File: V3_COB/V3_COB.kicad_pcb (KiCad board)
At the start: 4 copper layers, 16 x 16 mm, 3 parts, among them J101 Conn_02x35_Counter_Clockwise_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, J102 Conn_2Rows-76Pins

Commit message: XP update in V3_COB (clean up works)
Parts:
- removed J102: Conn_2Rows-76Pins, MOSBius_V2_CHIP:round_COB
- added J1: Conn_2Rows-76Pins, MOSBius_V2_CHIP:round_COB, F.Cu at (204.2, 63.5)
- moved G*** 2.25 mm to (211.2, 56.8)
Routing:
- net GND: track 46.7 -> 22.8 mm, vias 23 -> 4
- net /PIN 15: track 10.2 -> 6.47 mm
- net /PIN 13: track 10.1 -> 6.42 mm
- net /PIN 11: track 9.58 -> 6.14 mm
- net /PIN 56: track 8.49 -> 5.76 mm
- net /PIN 53: track 9.25 -> 6.63 mm
- net /PIN 12: track 7.82 -> 5.91 mm
- net /PIN 55: track 8.63 -> 7.02 mm
- net /PIN 41: track 7.76 -> 6.17 mm
- net /PIN 52: track 7.36 -> 5.84 mm
- net /PIN 46: track 6.46 -> 7.82 mm
- net /PIN 48: track 7.11 -> 5.94 mm
- net /PIN 44: track 7.13 -> 6.13 mm
- net /PIN 14: track 6.91 -> 6.07 mm
- net /PIN 45: track 5.92 -> 6.70 mm
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- added copper zone on In2.Cu, net GND
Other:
- board size 16 x 16 mm -> 18 x 16 mm
- board text removed: "Allocated Space For Passives"

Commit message: XP 5th March update
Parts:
- moved G*** 0.42 mm to (211.1, 57.2)
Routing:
- net GND: vias 4 -> 14
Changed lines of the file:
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@@
 	(footprint "Symbol:waferspace_pin1_silk"
 		(layer "F.Cu")
-		(at 211.166574 56.818292)
+		(at 211.106574 57.238292)
 		(property "Reference" "G***"
 			(at 0 0 0)
@@
 	)
 	(gr_line
+		(start 204.83 69.37)
+		(end 204.62 69.97)
+		(stroke
+			(width 0.2)
+			(type default)
+		)
+		(layer "F.Cu")
+		(net 21)
+	)
+	(gr_line
 		(start 209.59 64.41)
 		(end 211.01 64.6)
@@
 	)
 	(gr_line
+		(start 204.67 68.350625)
+		(end 204.83 69.37)
+		(stroke
+			(width 0.2)
+			(type default)
+		)
+		(layer "F.Cu")
+		(net 21)
+	)
+	(gr_line
 		(start 199.94 64.05)
 		(end 196.95 64.15)
@@
 	)
 	(gr_line
-		(start 204.69 68.44)
-		(end 204.83 69.13)
-		(stroke
-			(width 0.2)
-			(type default)
-		)
-		(layer "F.Cu")
-		(net 21)
-	)
-	(gr_line
 		(start 200.17 64.65)
 		(end 198.33 64.81)
@@
 	)
 	(gr_line
-		(start 204.83 69.13)
-		(end 204.19 70.56)
-		(stroke
-			(width 0.2)
-			(type default)
-		)
-		(layer "F.Cu")
-		(net 21)
-	)
-	(gr_line
 		(start 207.65 60.42)
 		(end 206.79 60.88)
@@
 	)
 	(segment
-		(start 204.165 70.555)
-		(end 204.16 70.56)
+		(start 204.16 68.655)
+		(end 204.16 69.54)
 		(width 0.3)
 		(layer "F.Cu")
@@
 	)
 	(segment
-		(start 204.165 68.635)
-		(end 204.165 70.555)
-		(width 0.25)
+		(start 204.16 69.54)
+		(end 204.63 70.01)
+		(width 0.3)
 		(layer "F.Cu")
 		(net 21)
 	)
 	(via
-		(at 204.16 70.56)
+		(at 204.63 70.01)
 		(size 0.45)
 		(drill 0.3)
@@
 	)
 	(segment
-		(start 203.335 70.3)
-		(end 202.805 70.3)
+		(start 204.34 70.3)
+		(end 204.63 70.01)
 		(width 0.2)
 		(layer "B.Cu")
@@
 	)
 	(segment
-		(start 203.595 70.56)
-		(end 203.335 70.3)
-		(width 0.2)
-		(layer "B.Cu")
-		(net 21)
-	)
-	(segment
-		(start 204.16 70.56)
-		(end 203.595 70.56)
+		(start 202.805 70.3)
+		(end 204.34 70.3)
 		(width 0.2)
 		(layer "B.Cu")
@@
 	)
 	(segment
-		(start 203.61 68.22)
-		(end 203.685 68.145)
-		(width 0.1)
-		(layer "F.Cu")
-		(net 37)
-	)
-	(segment
-		(start 203.62 69.88)
-		(end 203.61 69.87)
+		(start 203.61 69.54)
+		(end 203.61 68.22)
 		(width 0.1)
 		(layer "F.Cu")
@@
 	)
 	(segment
-		(start 203.61 69.87)
-		(end 203.61 68.22)
+		(start 203.61 68.22)
+		(end 203.685 68.145)
 		(width 0.1)
 		(layer "F.Cu")
@@
 	)
 	(via
-		(at 203.62 69.88)
+		(at 203.61 69.54)
 		(size 0.45)
 		(drill 0.3)
@@
 	)
 	(segment
-		(start 202.805 69.9)
-		(end 203.6 69.9)
+		(start 203.25 69.9)
+		(end 203.61 69.54)
 		(width 0.1)
 		(layer "B.Cu")
@@
 	)
 	(segment
-		(start 203.6 69.9)
-		(end 203.62 69.88)
+		(start 202.805 69.9)
+		(end 203.25 69.9)
 		(width 0.1)
 		(layer "B.Cu")
@@
 	)
 	(via
+		(at 209.55 69.07)
+		(size 0.45)
+		(drill 0.3)
+		(layers "F.Cu" "B.Cu")
+		(free yes)
+		(net 55)
+	)
+	(via
 		(at 210.795 67.84)
 		(size 0.45)
@@
 	)
 	(via
+		(at 196.17 57.72)
+		(size 0.45)
+		(drill 0.3)
+		(layers "F.Cu" "B.Cu")
+		(free yes)
+		(net 55)
+	)
+	(via
+		(at 197.48 70.31)
+		(size 0.45)
+		(drill 0.3)
+		(layers "F.Cu" "B.Cu")
+		(free yes)
+		(net 55)
+	)
+	(via
+		(at 198.62 68.98)
+		(size 0.45)
+		(drill 0.3)
+		(layers "F.Cu" "B.Cu")
+		(free yes)
+		(net 55)
+	)
+	(via
+		(at 204.1 70.999)
+		(size 0.5)
+		(drill 0.3)
+		(layers "F.Cu" "B.Cu")
+		(net 55)
+	)
+	(via
+		(at 196.37 69.21)
+		(size 0.45)
+		(drill 0.3)
+		(layers "F.Cu" "B.Cu")
+		(free yes)
+		(net 55)
+	)
+	(via
 		(at 210.45 58.22)
 		(size 0.45)
@@
 	)
 	(via
+		(at 210.49 70.51)
+		(size 0.45)
+		(drill 0.3)
+		(layers "F.Cu" "B.Cu")
+		(free yes)
+		(net 55)
+	)
+	(via
+		(at 197.27 56.61)
+		(size 0.45)
+		(drill 0.3)
+		(layers "F.Cu" "B.Cu")
+		(free yes)
+		(net 55)
+	)
+	(via
+		(at 212.06 69.97)
+		(size 0.45)
+		(drill 0.3)
+		(layers "F.Cu" "B.Cu")
+		(free yes)
+		(net 55)
+	)
+	(via
 		(at 197.57 67.87)
 		(size 0.45)
@@
 	)
 	(via
+		(at 204.25 56.225)
+		(size 0.45)
+		(drill 0.3)
+		(layers "F.Cu" "B.Cu")
+		(net 55)
+	)
+	(via
 		(at 198.27 58.06)
 		(size 0.45)
@@
 	(segment
 		(start 203.029 70.999)
-		(end 205.291 70.999)
+		(end 203.5 70.999)
 		(width 0.1)
 		(layer "B.Cu")
@@
 	(segment
 		(start 202.805 56.225)
-		(end 205.515 56.225)
+		(end 204.25 56.225)
 		(width 0.3)
 		(layer "B.Cu")
@@
 	)
 	(segment
+		(start 204.25 56.225)
+		(end 205.515 56.225)
+		(width 0.3)
+		(layer "B.Cu")
+		(net 55)
+	)
+	(segment
 		(start 202.805 70.775)
 		(end 202.674503 70.905497)
@@
 	)
 	(segment
+		(start 203.5 70.999)
+		(end 204.1 70.999)
+		(width 0.1)
+		(layer "B.Cu")
+		(net 55)
+	)
+	(segment
 		(start 205.515 56.225)
 		(end 205.46 56.17)
@@
 		(width 0.1)
 		(layer "B.Cu")
+		(net 55)
+	)
+	(segment
+		(start 204.1 70.999)
+		(end 205.291 70.999)
+		(width 0.1)
+		(layer "B.Cu")

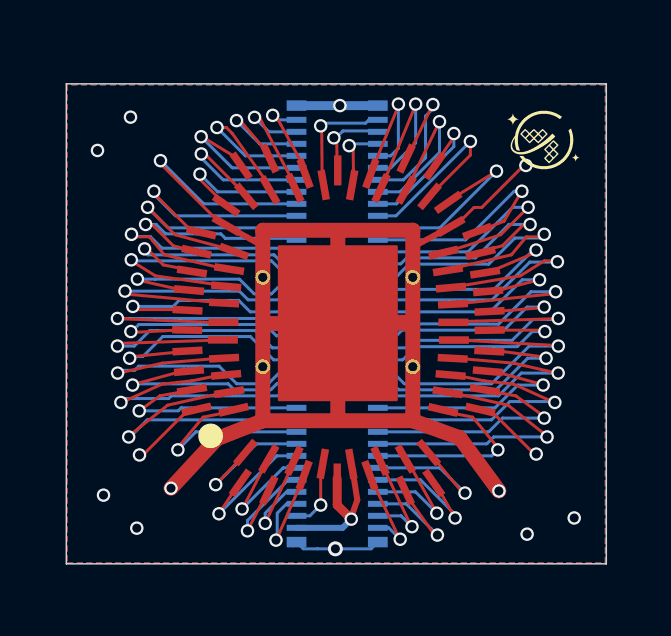
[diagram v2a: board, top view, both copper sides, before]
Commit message: XP update in layout for V3_COB
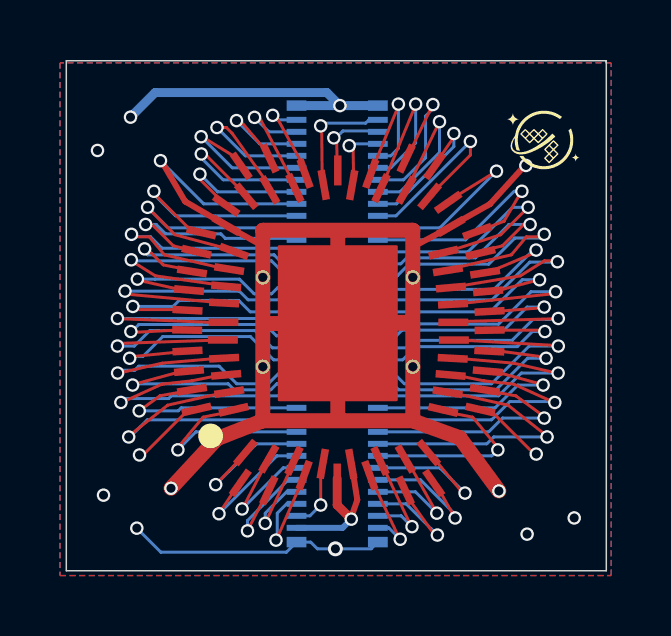
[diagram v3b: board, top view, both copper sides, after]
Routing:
- net GND: track 22.8 -> 29.8 mm
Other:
- board size 18 x 16 mm -> 18 x 17 mm
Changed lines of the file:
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@@
 		(grid_origin 180 65)
 		(pcbplotparams
-			(layerselection 0x00000000_00000000_55555555_5755f5ff)
-			(plot_on_all_layers_selection 0x00000000_00000000_00000000_00000000)
+			(layerselection 0x00000000_00000000_5555555f_fff5ffff)
+			(plot_on_all_layers_selection 0x00000000_00000000_0000000a_aaa0aaff)
 			(disableapertmacros no)
 			(usegerberextensions no)
@@
 			(outputformat 1)
 			(mirror no)
-			(drillshape 1)
+			(drillshape 0)
 			(scaleselection 1)
-			(outputdirectory "")
+			(outputdirectory "Gerber_Drill_Files/")
 		)
 	)
@@
 	)
 	(gr_line
+		(start 208.22 60.09)
+		(end 209.25 59.51)
+		(stroke
+			(width 0.2)
+			(type default)
+		)
+		(layer "F.Cu")
+		(net 55)
+	)
+	(gr_line
 		(start 208.25 67.3)
 		(end 209.55 69.07)
@@
 	)
 	(gr_line
+		(start 199.09 59.42)
+		(end 198.33 58.12)
+		(stroke
+			(width 0.2)
+			(type default)
+		)
+		(layer "F.Cu")
+		(net 55)
+	)
+	(gr_line
 		(start 200.17 64.65)
 		(end 198.33 64.81)
@@
 	)
 	(gr_line
+		(start 200.17 60.05)
+		(end 199.09 59.42)
+		(stroke
+			(width 0.2)
+			(type default)
+		)
+		(layer "F.Cu")
+		(net 55)
+	)
+	(gr_line
 		(start 200.25 65.21)
 		(end 199.31 65.4)
@@
 	)
 	(gr_line
+		(start 209.25 59.51)
+		(end 210.39 58.25)
+		(stroke
+			(width 0.2)
+			(type default)
+		)
+		(layer "F.Cu")
+		(net 55)
+	)
+	(gr_line
 		(start 200.3 62.8)
 		(end 197.04 62.5)
@@
 	)
 	(gr_rect
-		(start 195.13 55.5)
-		(end 213.13 71.5)
+		(start 195.13 54.73)
+		(end 213.13 71.73)
 		(stroke
 			(width 0.05)
-			(type default)
+			(type solid)
 		)
 		(fill no)
@@
 	(dimension
 		(type orthogonal)
-		(layer "Eco1.User")
+		(layer "User.1")
 		(pts
-			(xy 212.34 71.5) (xy 212.16 55.5)
+			(xy 213.13 71.73) (xy 213.13 54.73)
 		)
-		(height 2.18)
+		(height 3.87)
 		(orientation 1)
 		(format
@@
 			(units 3)
 			(units_format 1)
-			(precision 0)
+			(precision 4)
 		)
 		(style
 			(thickness 0.1)
 			(arrow_length 1.27)
-			(text_position_mode 2)
+			(text_position_mode 0)
 			(arrow_direction outward)
 			(extension_height 0.58642)
@@
 			(keep_text_aligned yes)
 		)
-		(gr_text "16 mm"
-			(at 215.57 63.589947 90)
-			(layer "Eco1.User")
+		(gr_text "17.0000 mm"
+			(at 215.85 63.23 90)
+			(layer "User.1")
 			(effects
 				(font
@@
 	)
 	(segment
-		(start 200.325 60.215)
-		(end 198.27 58.16)
-		(width 0.1)
-		(layer "F.Cu")
-		(net 55)
-	)
-	(segment
 		(start 210.45 58.26)
 		(end 210.45 58.22)
@@
 	)
 	(segment
-		(start 208.085 60.255)
-		(end 208.72 59.62)
-		(width 0.1)
-		(layer "F.Cu")
-		(net 55)
-	)
-	(segment
-		(start 208.72 59.62)
-		(end 208.98 59.62)
-		(width 0.1)
-		(layer "F.Cu")
-		(net 55)
-	)
-	(segment
 		(start 199.205 66.355)
 		(end 197.69 67.87)
@@
 	)
 	(segment
-		(start 208.98 59.62)
-		(end 210.38 58.22)
-		(width 0.1)
-		(layer "F.Cu")
-		(net 55)
-	)
-	(segment
 		(start 199.47 66.355)
 		(end 199.205 66.355)
@@
 	)
 	(segment
-		(start 203.029 70.999)
-		(end 203.5 70.999)
+		(start 202.805 56.225)
+		(end 202.694 56.114)
 		(width 0.1)
 		(layer "B.Cu")
@@
 	)
 	(segment
-		(start 202.805 56.225)
-		(end 202.694 56.114)
+		(start 198.09 55.79)
+		(end 197.27 56.61)
+		(width 0.3)
+		(layer "B.Cu")
+		(net 55)
+	)
+	(segment
+		(start 198.281 71.111)
+		(end 197.48 70.31)
 		(width 0.1)
 		(layer "B.Cu")
@@
 	)
 	(segment
+		(start 203.276 70.775)
+		(end 203.5 70.999)
+		(width 0.1)
+		(layer "B.Cu")
+		(net 55)
+	)
+	(segment
 		(start 205.291 70.999)
 		(end 205.515 70.775)
@@
 	)
 	(segment
-		(start 202.805 70.775)
-		(end 202.674503 70.905497)
+		(start 202.805 59.5)
+		(end 199.71 59.5)
 		(width 0.1)
 		(layer "B.Cu")
@@
 	)
 	(segment
-		(start 202.805 59.5)
-		(end 199.71 59.5)
-		(width 0.1)
+		(start 203.815 55.79)
+		(end 198.09 55.79)
+		(width 0.3)
 		(layer "B.Cu")
 		(net 55)
@@
 	(segment
 		(start 202.805 70.775)
-		(end 203.029 70.999)
+		(end 202.469 71.111)
 		(width 0.1)
 		(layer "B.Cu")
@@
 	)
 	(segment
+		(start 202.805 70.775)
+		(end 203.276 70.775)
+		(width 0.1)
+		(layer "B.Cu")
+		(net 55)
+	)
+	(segment
 		(start 202.86 56.17)
 		(end 202.805 56.225)
@@
 	)
 	(segment
+		(start 202.469 71.111)
+		(end 198.281 71.111)
+		(width 0.1)
+		(layer "B.Cu")
+		(net 55)
+	)
+	(segment
+		(start 204.25 56.225)
+		(end 203.815 55.79)
+		(width 0.3)
+		(layer "B.Cu")
+		(net 55)
+	)
+	(segment
 		(start 199.71 59.5)
 		(end 198.27 58.06)
@@
 		(polygon
 			(pts
-				(xy 195.16 55.53) (xy 195.16 71.47) (xy 213.1 71.47) (xy 213.1 55.53)
+				(xy 194.92 54.8) (xy 194.92 71.89) (xy 213.29 71.89) (xy 213.29 54.8)
 			)
 		)
